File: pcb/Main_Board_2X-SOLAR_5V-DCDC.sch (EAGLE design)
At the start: 72 parts, among them CN5 USBA_FEMALE, M3AB FDMC8030, T2 MMUN2133LT1G, U1 LTC4015EUHFPBFQFN-38_UHF-M, U3 TPS61090RSAR, X1 6V_PV

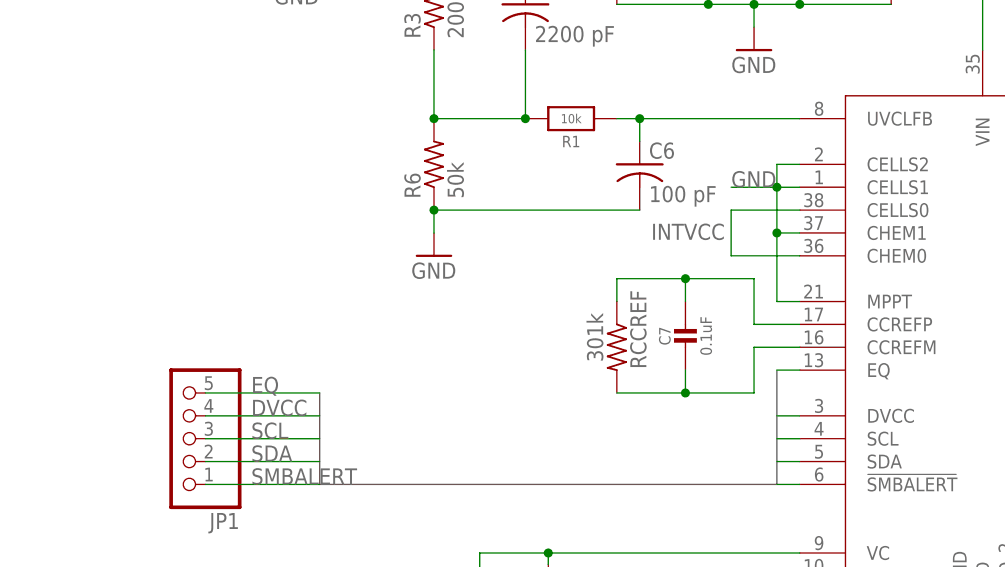
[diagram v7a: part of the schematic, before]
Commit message: Sentinel Board V1P3
Updated silkscreen and added MPPT switch to allow for logic level/pin selection for MPPT instead of i2c only.
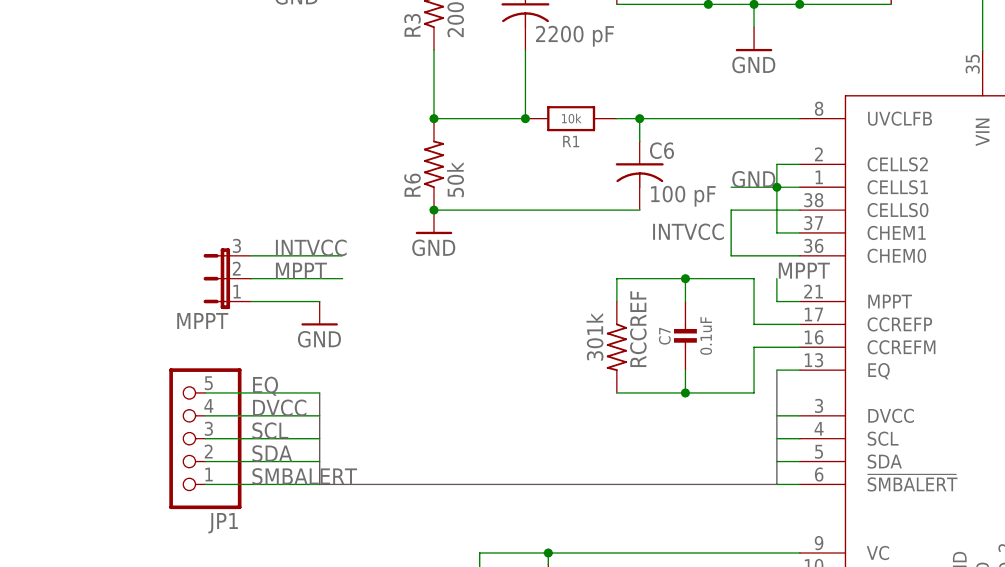
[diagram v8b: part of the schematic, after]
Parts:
- added MPPT: (no value), jumper:JP2E
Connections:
- new net MPPT: MPPT.2, U1.MPPT
- net GND: now also MPPT.1; no longer U1.MPPT
- net INTVCC: now also MPPT.3
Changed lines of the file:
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@@
 <?xml version="1.0" encoding="utf-8"?>
 <!DOCTYPE eagle SYSTEM "eagle.dtd">
-<eagle version="8.3.1">
+<eagle version="8.3.2">
 <drawing>
 <settings>
@@
 <part name="C31" library="adafruit" library_urn="urn:adsk.eagle:library:420" deviceset="C-US" device="C0805" value="2200 pF"/>
 <part name="RNTC" library="microbuilder" deviceset="RESISTOR" device="_0805MP" value="10k"/>
+<part name="MPPT" library="jumper" library_urn="urn:adsk.eagle:library:252" deviceset="JP2E" device="" package3d_urn="urn:adsk.eagle:package:15452/1"/>
+<part name="GND2" library="supply1" library_urn="urn:adsk.eagle:library:371" deviceset="GND" device=""/>
 </parts>
 <sheets>
@@
 <instance part="C6" gate="G$1" x="91.44" y="152.4"/>
 <instance part="R6" gate="G$1" x="68.58" y="152.4" rot="R90"/>
-<instance part="GND3" gate="1" x="68.58" y="142.24"/>
+<instance part="GND3" gate="1" x="68.58" y="144.78"/>
 <instance part="GND5" gate="1" x="104.14" y="165.1"/>
 <instance part="RCCREF" gate="G$1" x="88.9" y="132.08" smashed="yes" rot="R270">
@@
 <instance part="C31" gate="G$1" x="78.74" y="170.18"/>
 <instance part="RNTC" gate="G$1" x="157.48" y="86.36" rot="R90"/>
+<instance part="MPPT" gate="1" x="45.72" y="139.7" rot="R90"/>
+<instance part="GND2" gate="1" x="55.88" y="134.62"/>
 </instances>
 <busses>
@@
 <wire x1="91.44" y1="147.32" x2="68.58" y2="147.32" width="0.1524" layer="91"/>
 <junction x="68.58" y="147.32"/>
-<wire x1="68.58" y1="147.32" x2="68.58" y2="144.78" width="0.1524" layer="91"/>
 </segment>
 <segment>
@@
 <pinref part="U1" gate="A" pin="CHEM1"/>
 <wire x1="106.68" y1="144.78" x2="109.22" y2="144.78" width="0.1524" layer="91"/>
-<wire x1="106.68" y1="144.78" x2="106.68" y2="137.16" width="0.1524" layer="91"/>
-<junction x="106.68" y="144.78"/>
-<pinref part="U1" gate="A" pin="MPPT"/>
-<wire x1="106.68" y1="137.16" x2="109.22" y2="137.16" width="0.1524" layer="91"/>
 <wire x1="106.68" y1="149.86" x2="106.68" y2="152.4" width="0.1524" layer="91"/>
 <pinref part="U1" gate="A" pin="CELLS2"/>
@@
 <pinref part="RNTC" gate="G$1" pin="1"/>
 <wire x1="157.48" y1="78.74" x2="157.48" y2="81.28" width="0.1524" layer="91"/>
+</segment>
+<segment>
+<pinref part="MPPT" gate="1" pin="1"/>
+<wire x1="48.26" y1="137.16" x2="55.88" y2="137.16" width="0.1524" layer="91"/>
+<pinref part="GND2" gate="1" pin="GND"/>
 </segment>
 </net>
@@
 <label x="92.71" y="144.018" size="1.778" layer="95"/>
 </segment>
+<segment>
+<pinref part="MPPT" gate="1" pin="3"/>
+<wire x1="48.26" y1="142.24" x2="58.42" y2="142.24" width="0.1524" layer="91"/>
+<label x="50.8" y="142.24" size="1.778" layer="95"/>
+</segment>
 </net>
 <net name="UVCLFB" class="0">
@@
 </segment>
 </net>
+<net name="MPPT" class="0">
+<segment>
+<pinref part="U1" gate="A" pin="MPPT"/>
+<wire x1="106.68" y1="137.16" x2="109.22" y2="137.16" width="0.1524" layer="91"/>
+<wire x1="106.68" y1="137.16" x2="106.68" y2="139.7" width="0.1524" layer="91"/>
+<label x="106.68" y="139.7" size="1.778" layer="95"/>
+</segment>
+<segment>
+<wire x1="58.42" y1="139.7" x2="48.26" y2="139.7" width="0.1524" layer="91"/>
+<pinref part="MPPT" gate="1" pin="2"/>
+<label x="50.8" y="139.7" size="1.778" layer="95"/>
+</segment>
+</net>
 </nets>
 </sheet>
@@
 with this version.
 </note>
+<note version="8.3" severity="warning">
+Since Version 8.3, EAGLE supports URNs for individual library
+assets (packages, symbols, and devices). The URNs of those assets
+will not be understood (or retained) with this version.
+</note>
+<note version="8.3" severity="warning">
+Since Version 8.3, EAGLE supports the association of 3D packages
+with devices in libraries, schematics, and board files. Those 3D
+packages will not be understood (or retained) with this version.
+</note>
 </compatibility>
